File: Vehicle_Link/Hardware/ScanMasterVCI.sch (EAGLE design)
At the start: 83 parts, among them IC1 XMEGA32A4U, Q1 MMBT4403, Q10 ZXMP6A17G, Q2 MMBT3904, Q3 MMBT3904, Q4 MMBT3904, Q5 MMBT3904, Q6 MMBT3904, U1 L78L08ABUTR, U2 MAX13444EASA+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

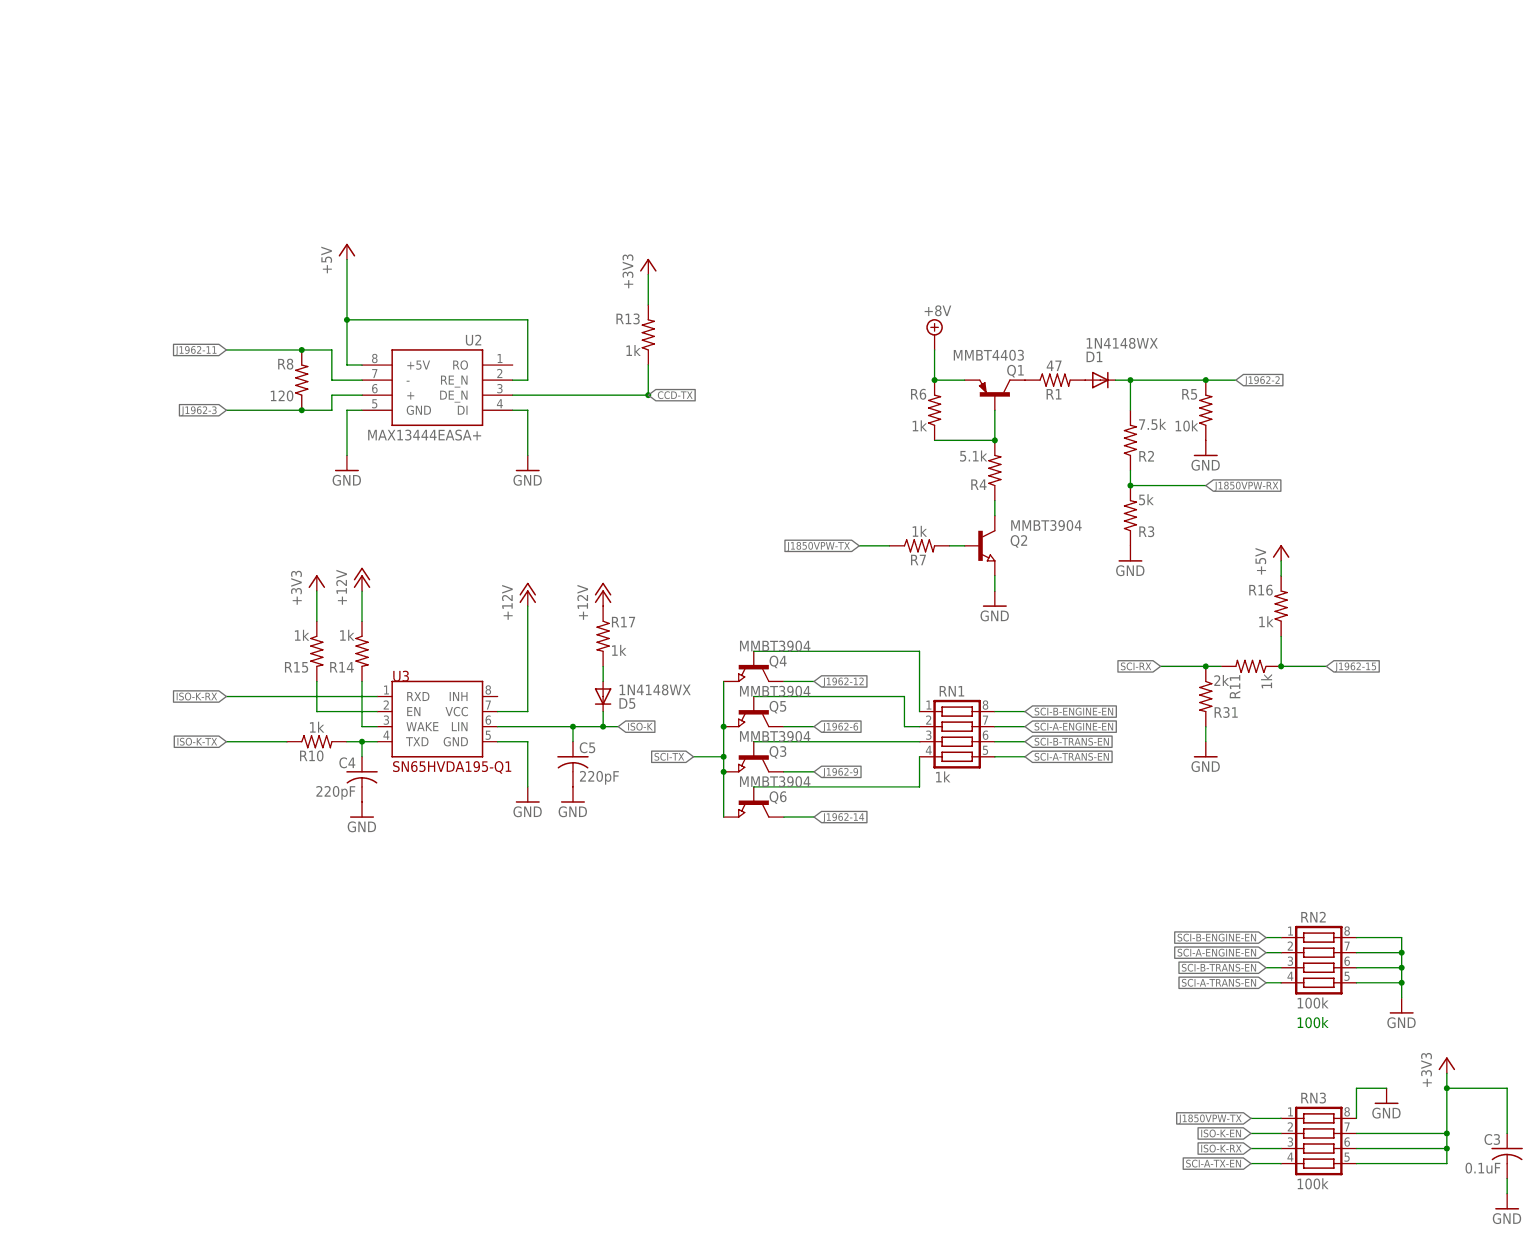
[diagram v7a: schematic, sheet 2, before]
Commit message: Based on testing I did previously, added new circuits to hopefully finish out the CCD, SCI, and ISO9141. J1850 still needs work.
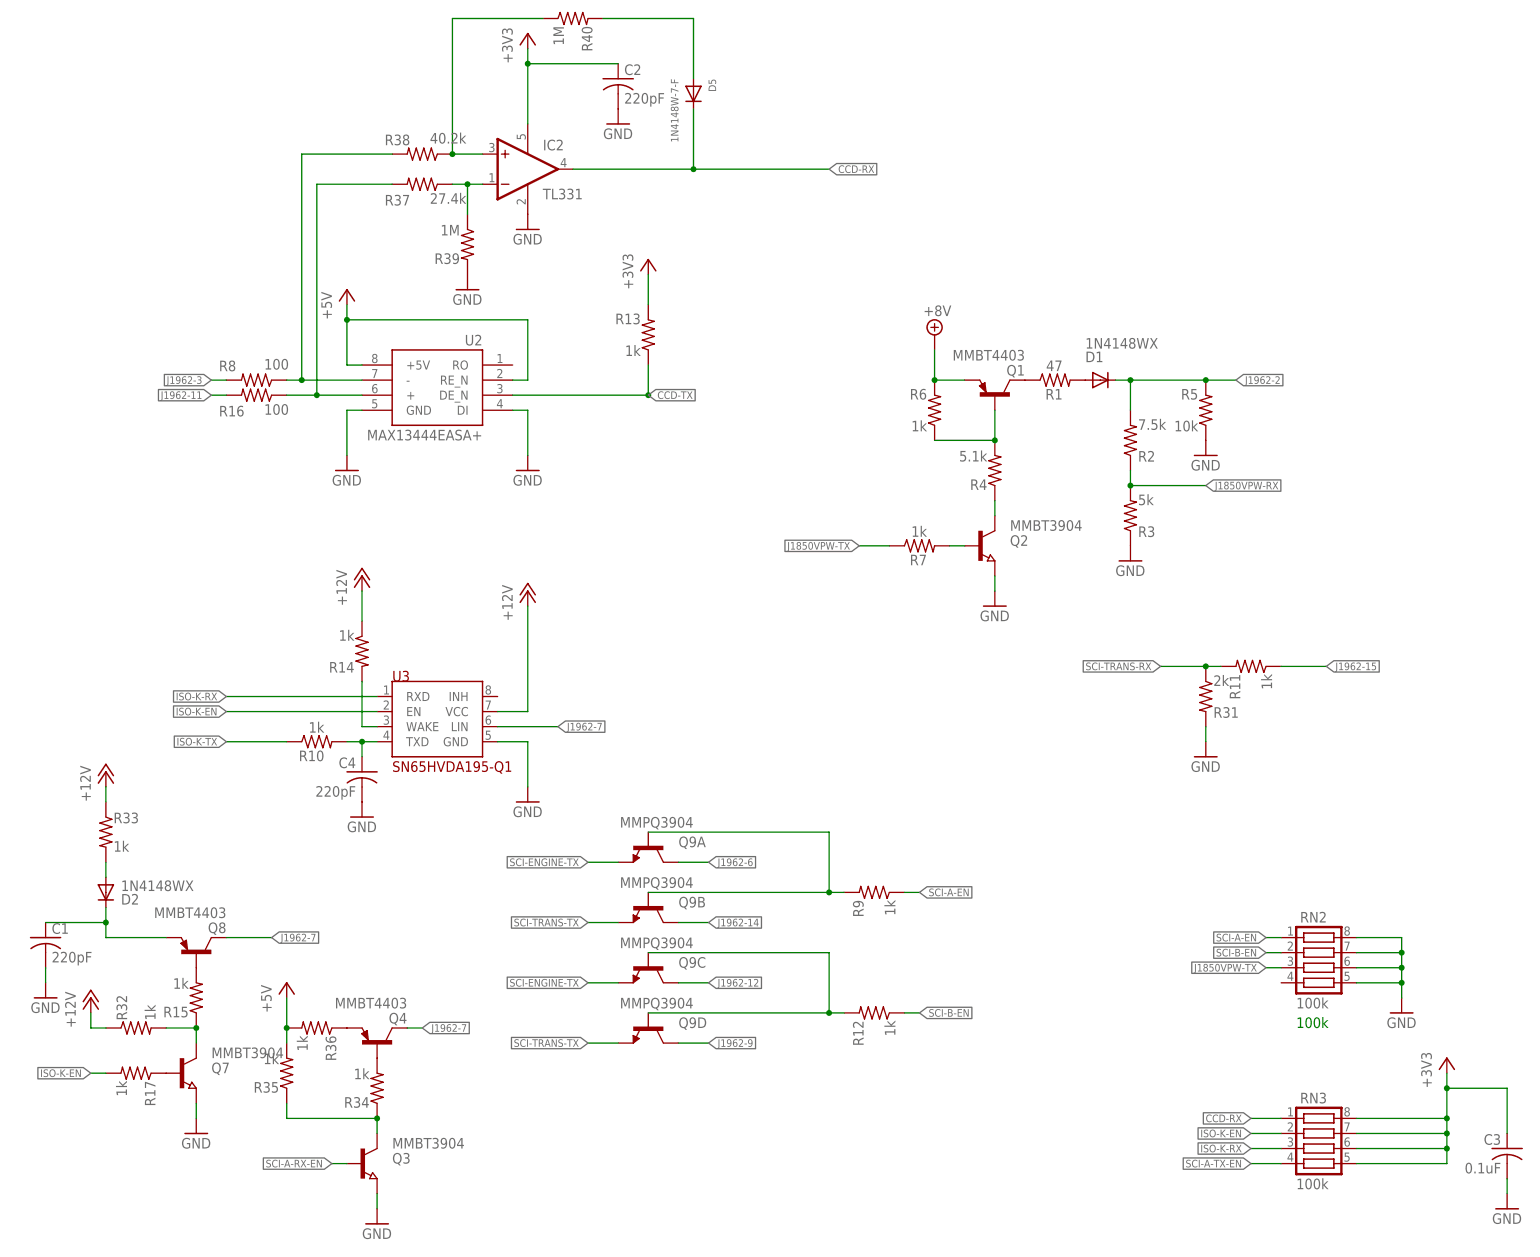
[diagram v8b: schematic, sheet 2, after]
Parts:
- removed C5: 220pF, adafruit:C-USC0603
- removed Q5, Q6: MMBT3904, semicon-smd-ipc:NPN-TRANSISTOR_SOT23
- removed RN1: 1k, resistor-net:CTS742C083
- added C1, C2: 220pF, adafruit:C-USC0603
- added D2: 1N4148WX, diode:DIODE-SOD323-R
- added IC2: TL331, linear:TL331
- added Q7: MMBT3904, semicon-smd-ipc:NPN-TRANSISTOR_SOT23
- added Q8: MMBT4403, transistor-pnp:MMBT4403LT1SMD
- added Q9: MMPQ3904, customics:MMPQ3904
- added R12, R32, R33, R34, R35, R36, R9: 1k, adafruit:R-US_R0603
- added R37: 27.4k, adafruit:R-US_R0603
- added R38: 40.2k, adafruit:R-US_R0603
- added R39, R40: 1M, adafruit:R-US_R0603
- D5: value 1N4148WX -> 1N4148W-7-F; device diode:DIODE-SOD323-R -> customics:1N4148W-7-F
- Q4: value MMBT3904 -> MMBT4403; device semicon-smd-ipc:NPN-TRANSISTOR_SOT23 -> transistor-pnp:MMBT4403LT1SMD
- R16: value 1k -> 100
- R8: value 120 -> 100
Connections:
- removed net ISO-K: C5.1, D5.C, U3.LIN
- removed net SCI-RX: IC1.PE2, R11.2, R31.1
- removed net SCI-TX: IC1.PE3, Q3.E, Q4.E, Q5.E, Q6.E
- new net N$1: Q9A.B, Q9B.B, R9.2
- new net N$11: D2.A, R33.2
- new net N$32: R16.1, R37.2, U2.+
- new net N$33: R38.2, R8.1, U2.-
- new net N$34: IC2.-IN, R37.1, R39.1
- new net N$35: IC2.+IN, R38.1, R40.1
- new net N$36: D5.A, R40.2
- new net N$4: Q7.C, R15.1, R32.2
- new net N$5: Q9C.B, Q9D.B, R12.2
- new net SCI-A-EN: R9.1, RN2.1
- new net SCI-A-RX-EN: IC1.PC4, Q3.B
- new net SCI-B-EN: R12.1, RN2.2
- new net SCI-B-RX-EN: IC1.PC5
- new net SCI-ENGINE-RX: IC1.PE2
- new net SCI-ENGINE-TX: IC1.PE3, Q9A.E, Q9C.E
- new net SCI-TRANS-RX: IC1.PC6, R11.2, R31.1
- new net SCI-TRANS-TX: IC1.PC7, Q9B.E, Q9D.E
- net +12V: now also R32.1, R33.1; no longer R17.1
- net +3V3: now also C2.1, IC2.V+, RN3.8; no longer R15.1
- net +5V: now also R35.2, R36.2; no longer R16.2
- net CCD-RX: now also D5.C, IC2.OUT, RN3.1
- net GND: now also C1.2, C2.2, IC2.GND, Q3.E, Q7.E, R39.2; no longer C5.2, RN3.8
- net ISO-K-EN: now also R17.2, U3.EN
- net J1850VPW-TX: now also RN2.3; no longer RN3.1
- net J1962-11: now also R16.2; no longer R8.2, U2.-
- net J1962-12: now also Q9C.C; no longer Q4.C
- net J1962-14: now also Q9B.C; no longer Q6.C
- net J1962-15: no longer R16.1
- net J1962-3: now also R8.2; no longer R8.1, U2.+
- net J1962-6: now also Q9A.C; no longer Q5.C
- net J1962-7: now also Q4.C, Q8.C, U3.LIN
- net J1962-9: now also Q9D.C; no longer Q3.C
- net N$13: now also Q7.B, R17.1; no longer Q4.B, RN1.1
- net N$21: now also C1.1, D2.C, Q8.E; no longer Q5.B, RN1.2
- net N$22: now also Q4.B, R34.2; no longer Q3.B, RN1.3
- net N$23: now also Q3.C, R34.1, R35.1; no longer Q6.B, RN1.4
- net N$31: now also Q4.E, R36.1; no longer D5.A, R17.2
- net N$8: now also Q8.B; no longer U3.EN
- net SCI-A-ENGINE-EN: no longer RN1.7, RN2.2
- net SCI-A-TRANS-EN: no longer RN1.5, RN2.4
- net SCI-B-ENGINE-EN: no longer RN1.8, RN2.1
- net SCI-B-TRANS-EN: no longer RN1.6, RN2.3
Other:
- moved on the sheet: D5, Q3, R15, R16, R17, R8
